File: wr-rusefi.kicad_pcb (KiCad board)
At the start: 2 copper layers, 94 x 94 mm, 147 parts, among them P101 USB_OTG, P102 CONN_01X08, P103 CONN_01X08, P104 CONN_01X04, P105 CONN_01X08, P106 CONN_01X08, P107 CONN_01X02, P108 USB_OTG, P109 CONN_01X02, P110 CONN_01X06, Q401 IRF540N, Q402 IRF540N, Q403 IRF540N, Q404 IRF540N, Q405 IRF540N, Q406 IRF540N, U101 ISL89410, U102 ISL89410, U103 FT230XS, U104 MAX9924, U105 MCP2562-E/SN, U106 LD1117S33TR, U107 MAX9924, U108 ISL89410, U109 STM32F407VGTx, U110 ISL89410, U201 LM324, U301 LM324, U501 LM7805CT, Y101 Crystal

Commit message: Mostly done new layout
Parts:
- C104, C105, C107, C108, C110, C114, C115, C116, C117, C205, C305, D109, U106: moved to B.Cu
- moved C105 154.2 mm to (118.1, 106.0), turned to 180 degrees
- moved D109 146.1 mm to (74.9, 104.1), turned to 180 degrees
- moved C502 145.4 mm to (109.2, 108.0)
- moved C501 145.1 mm to (93.3, 108.0)
- moved U501 144.5 mm to (102.9, 111.1)
- moved U106 143.6 mm to (118.1, 100.3)
- moved C104 133.5 mm to (118.1, 94.6)
- moved D103 128.2 mm to (132.7, 138.4), turned to 90 degrees
- moved U107 123.4 mm to (115.6, 140.3), turned to 270 degrees
- moved R120 121.8 mm to (117.5, 132.7), turned to 90 degrees
- moved C106 121.4 mm to (116.2, 135.9), turned to 180 degrees
- moved R105 119.5 mm to (117.5, 127.0), turned to 90 degrees
- moved R121 118.4 mm to (114.9, 132.7), turned to 90 degrees
- moved P104 118.4 mm to (117.5, 122.6), turned to 180 degrees
- moved U104 116.9 mm to (110.5, 140.3), turned to 270 degrees
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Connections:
- U109 pad 55: ls_4 -> ls_2
- U109 pad 56: ls_2 -> ls_1
- U109 pad 57: ls_3 -> ls_4
- U109 pad 58: ls_1 -> ls_3
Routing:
- net +5V: track 0.00 -> 239.3 mm, vias 0 -> 18
- net GND: track 159.7 -> 28.5 mm, vias 160 -> 9
- net +12V: track 0.00 -> 95.9 mm, vias 0 -> 2
- net VRIN2: track 0.00 -> 69.1 mm, vias 0 -> 2
- net ls_1: track 1.52 -> 69.8 mm, vias 0 -> 2
- net ls_2: track 1.52 -> 61.9 mm, vias 0 -> 2
- net VRIN1: track 0.00 -> 53.0 mm, vias 0 -> 2
- net INJ_A_IN: track 1.52 -> 54.3 mm, vias 0 -> 2
- net ls_3: track 1.52 -> 54.1 mm, vias 0 -> 2
- net INJ_B_IN: track 1.52 -> 53.5 mm, vias 0 -> 2
- net ls_4: track 1.52 -> 46.0 mm, vias 0 -> 2
- net VBUS: track 0.00 -> 41.8 mm, vias 0 -> 2
- net IGN_H_IN: track 0.00 -> 40.6 mm
- net IGN_G_IN: track 0.00 -> 39.8 mm
- net IGN_F_IN: track 0.00 -> 38.9 mm
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- added copper zone on B.Cu, net +3V3
- added copper zone on B.Cu, net +5V
- added copper zone on B.Cu, net Net-(C111-Pad6)
- added copper zone on B.Cu, net inj_a
- added copper zone on B.Cu, net inj_b
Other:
- net class Default: clearance 0.3048 -> 0.2032; trace_width 0.3048 -> 0.2032
- net class Ign out added: clearance 0.3048, trace_width 1.016, via_dia 0.6858, via_drill 0.3302
- rule trace_clearance: 0.3048 -> 0.2032

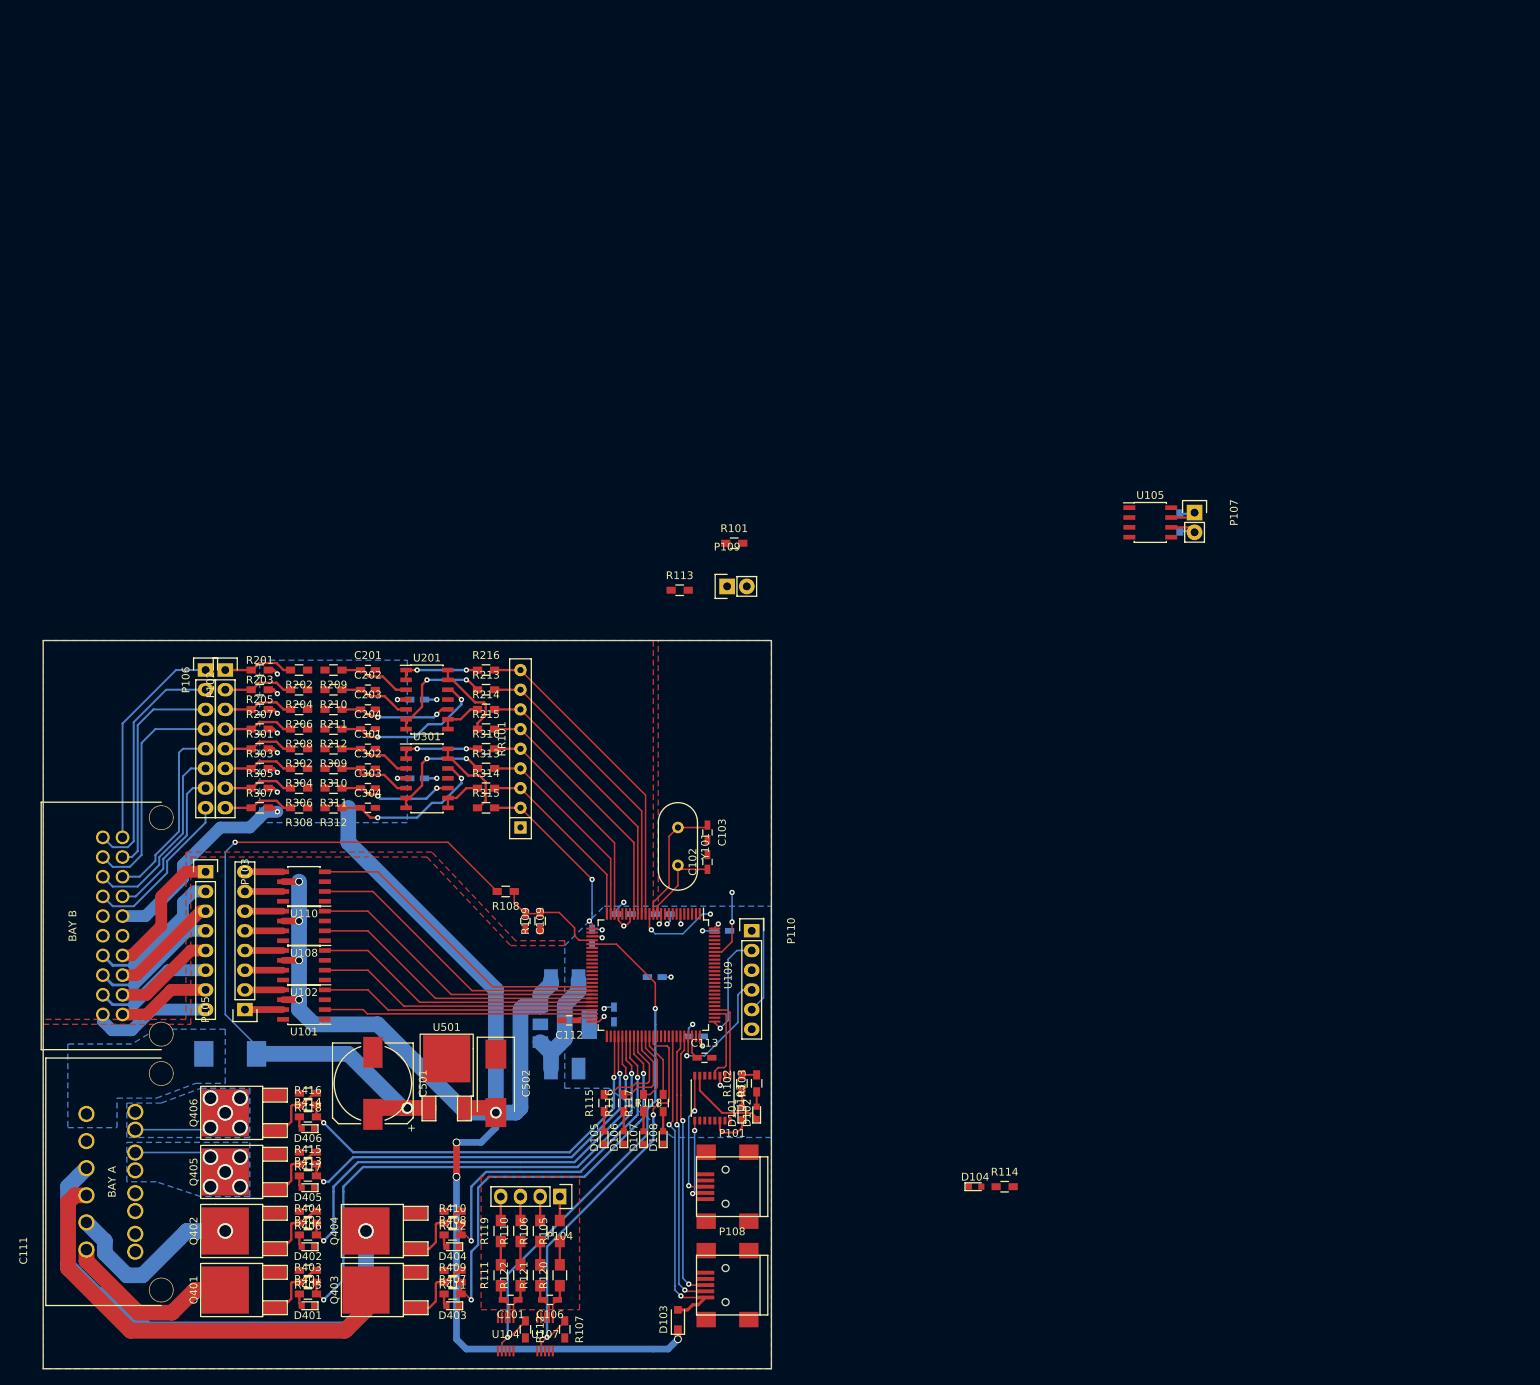
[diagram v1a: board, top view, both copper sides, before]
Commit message: Add rear ground pour
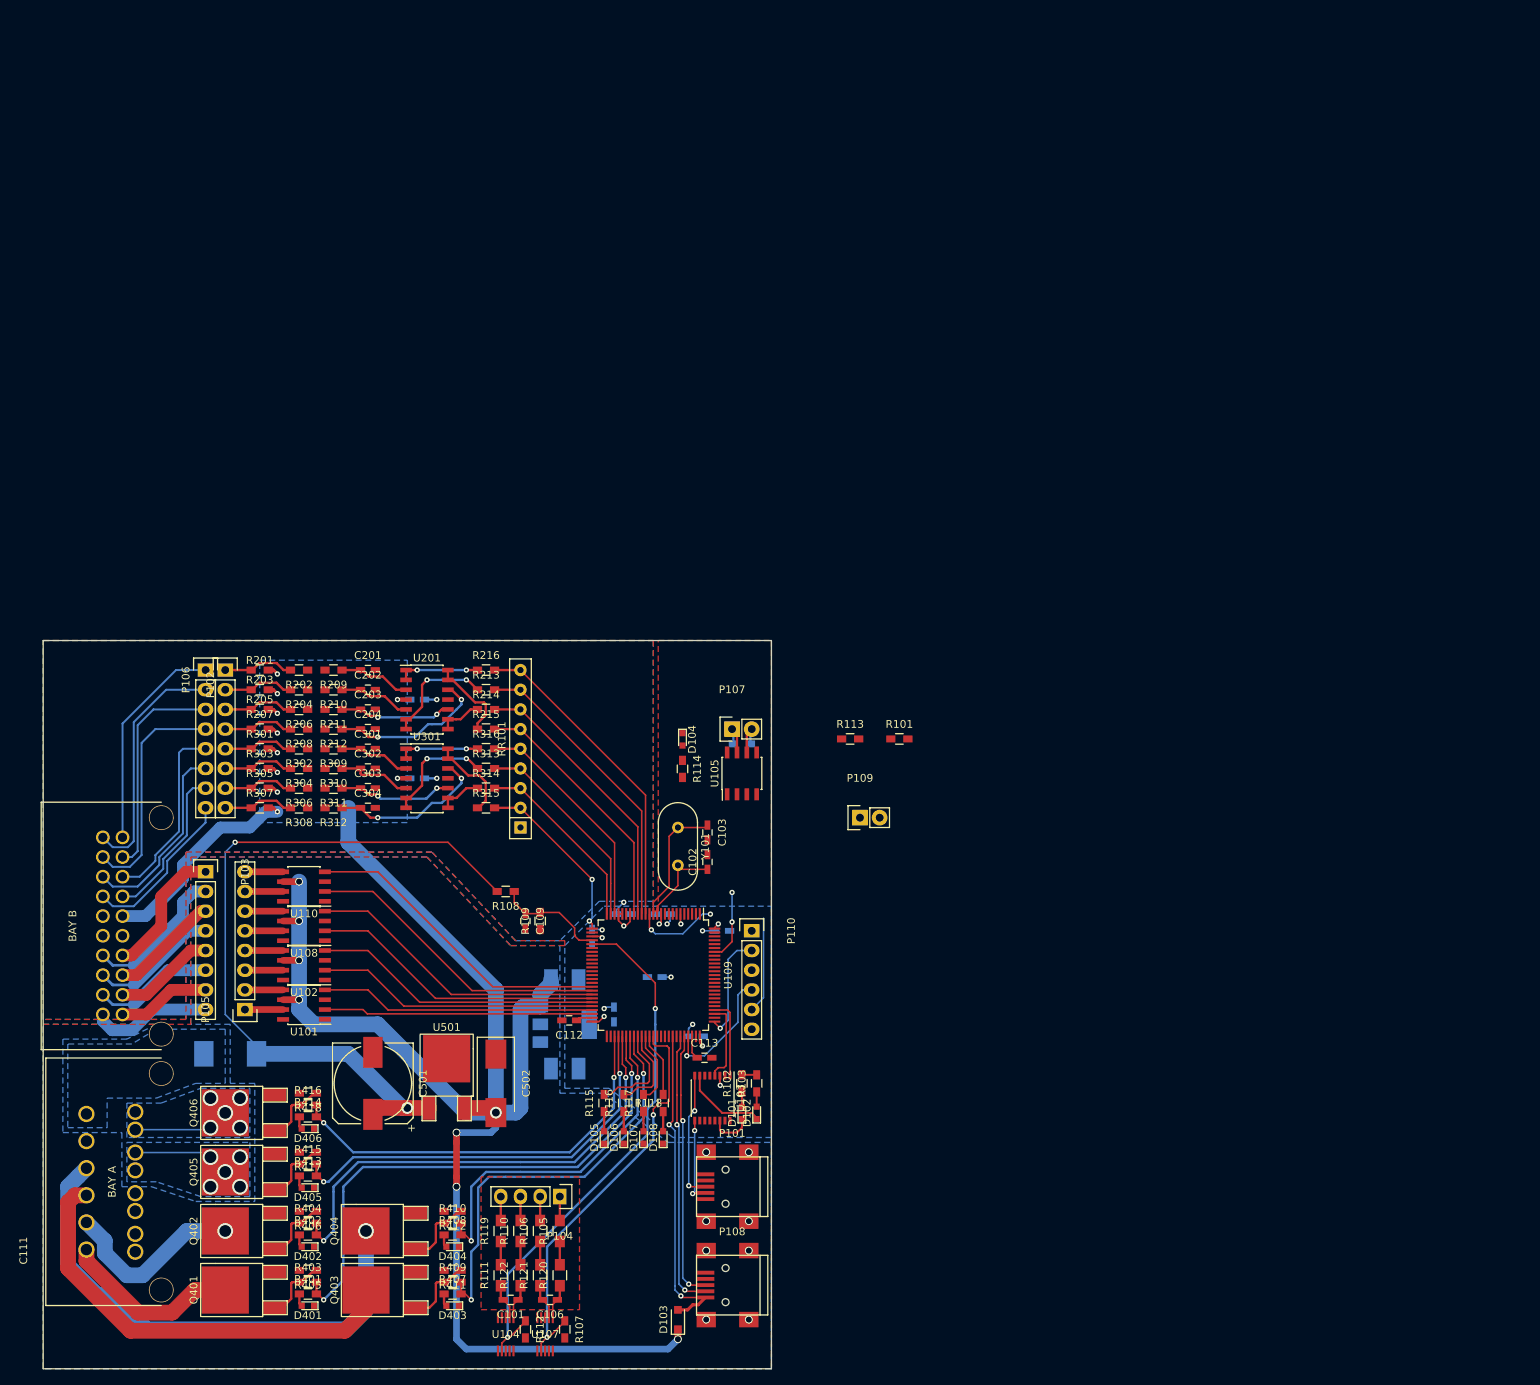
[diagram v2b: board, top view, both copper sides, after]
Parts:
- moved D104 69.0 mm to (133.3, 63.6), turned to 270 degrees
- moved R114 68.1 mm to (133.3, 67.4), turned to 270 degrees
- moved P107 65.9 mm to (139.7, 62.2), turned to 0 degrees
- moved R104 63.3 mm to (141.0, 64.1), turned to 180 degrees
- moved U105 61.9 mm to (141.0, 67.9), turned to 90 degrees
- moved P109 34.4 mm to (156.2, 73.7)
- moved R101 33.0 mm to (161.3, 63.5)
- moved R113 29.2 mm to (154.9, 63.5)
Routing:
- net GND: track 28.5 -> 13.7 mm, vias 9 -> 17
- net +5V: track 239.3 -> 240.0 mm
- added copper zone on B.Cu, net GND
